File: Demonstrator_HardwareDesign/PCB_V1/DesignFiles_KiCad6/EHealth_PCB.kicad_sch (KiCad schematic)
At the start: 24 parts, among them J1-AnalogSensors1 Conn_01x05, J3-MagneticInterconnect1 Conn_01x08, J4-OffTheShelf-Digital1 Conn_02x06_Counter_Clockwise, J5-Power1 Conn_01x03

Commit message: aangepaste pcb layout
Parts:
- removed J1-AnalogSensors1: Conn_01x05, Connector_PinHeader_2.54mm:PinHeader_1x05_P2.54mm_Vertical, symbol Connector_Generic:Conn_01x05
- removed R10, R11, R12, R5, R6, R7, R8, R9: R, Resistor_SMD:R_0805_2012Metric_Pad1.20x1.40mm_HandSolder, symbol Device:R
- added J1: Conn_01x06, Connector_PinHeader_2.54mm:PinHeader_2x04_P2.54mm_Vertical, symbol Connector_Generic:Conn_01x08
- added R16, R17, R21, R22: R, Resistor_SMD:R_0805_2012Metric_Pad1.20x1.40mm_HandSolder, symbol Device:R
- J3-MagneticInterconnect1: footprint Connector_JST:JST_VH_B8P-VH-B_1x08_P3.96mm_Vertical -> Connector_JST:JST_VH_B4P-VH-B_1x04_P3.96mm_Vertical; symbol Connector_Generic:Conn_01x08 -> Connector_Generic:Conn_01x04
- J4-OffTheShelf-Digital1: footprint Connector_PinSocket_2.54mm:PinSocket_2x06_P2.54mm_Vertical -> Connector_PinSocket_2.54mm:PinSocket_2x04_P2.54mm_Vertical; symbol Connector_Generic:Conn_02x06_Counter_Clockwise -> Connector_Generic:Conn_02x04_Counter_Clockwise
- renumbered R16 to R18, R17 to R19, R18 to R20
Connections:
- net +3.3V: now also J1.1 (Pin_1), R16.2, R17.2
- net GND: now also J1.2 (Pin_2), J1.8 (Pin_8), R21.2, R22.2
- net SPI_CS: no longer J3-MagneticInterconnect1.8 (Pin_8), J4-OffTheShelf-Digital1.9 (Pin_9)
- net SPI_MISO: now also J1.7 (Pin_7), R17.1, R22.1; no longer J3-MagneticInterconnect1.5 (Pin_5), J4-OffTheShelf-Digital1.12 (Pin_12)
- net SPI_MOSI: now also R13.1, R18.1, J1.6 (Pin_6); no longer J3-MagneticInterconnect1.6 (Pin_6), J4-OffTheShelf-Digital1.11 (Pin_11)
- net SPI_SCK: now also J1.3 (Pin_3), R16.1, R21.1; no longer J3-MagneticInterconnect1.7 (Pin_7), J4-OffTheShelf-Digital1.10 (Pin_10)
- net at LOLIN_C3_PICO1.10 (3_-_A3_-_VBAT), R14.1, R19.1: now also J1.5 (Pin_5)
- net at LOLIN_C3_PICO1.11 (2_-_A2), R15.1, R20.1: now also J1.4 (Pin_4)
- now unconnected: LOLIN_C3_PICO1.15 (5_-_A5)
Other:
- moved on the sheet: C1, C2, J5-Power1, LOLIN_C3_PICO1, R1, R13, R14, R15, R18, R19, R2, R20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

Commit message: aangepaste layout
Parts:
- removed R1, R18, R19, R20, R21, R22: R, Resistor_SMD:R_0805_2012Metric_Pad1.20x1.40mm_HandSolder, symbol Device:R
- J1: footprint Connector_PinHeader_2.54mm:PinHeader_2x04_P2.54mm_Vertical -> Connector_PinHeader_2.54mm:PinHeader_2x05_P2.54mm_Vertical; symbol Connector_Generic:Conn_01x08 -> Connector_Generic:Conn_01x10
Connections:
- net +3.3V: no longer J1.1 (Pin_1), J3-MagneticInterconnect1.1 (Pin_1)
- net GND: now also J1.1 (Pin_1), J1.3 (Pin_3), J1.5 (Pin_5), J1.7 (Pin_7), J1.9 (Pin_9); no longer J1.2 (Pin_2), J1.8 (Pin_8)
- net SPI_CS: now also J4-OffTheShelf-Digital1.5 (Pin_5)
- net SPI_MISO: no longer J1.7 (Pin_7), LOLIN_C3_PICO1.13 (0_-_A0_-_MISO), R17.1
- net at LOLIN_C3_PICO1.10 (3_-_A3_-_VBAT), R14.1: now also J1.8 (Pin_8); no longer J1.5 (Pin_5)
- net at LOLIN_C3_PICO1.11 (2_-_A2), R15.1: now also J1.6 (Pin_6); no longer J1.4 (Pin_4)
- net SPI_MOSI: no longer names the net of LOLIN_C3_PICO1.14 (4_-_A4_-_MOSI), R13.1
- net SPI_MOSI: now also J1.10 (Pin_10); no longer J1.6 (Pin_6)
- net SPI_SCK: no longer names the net of LOLIN_C3_PICO1.12 (1_-_A1_-_SCK), R16.1
- net SPI_SCK: now also J1.4 (Pin_4); no longer J1.3 (Pin_3)
- new net: J1.2 (Pin_2), LOLIN_C3_PICO1.13 (0_-_A0_-_MISO), R17.1
- new net Vdd: J3-MagneticInterconnect1.1 (Pin_1)
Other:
- moved on the sheet: R13, R14, R15, R16, R17

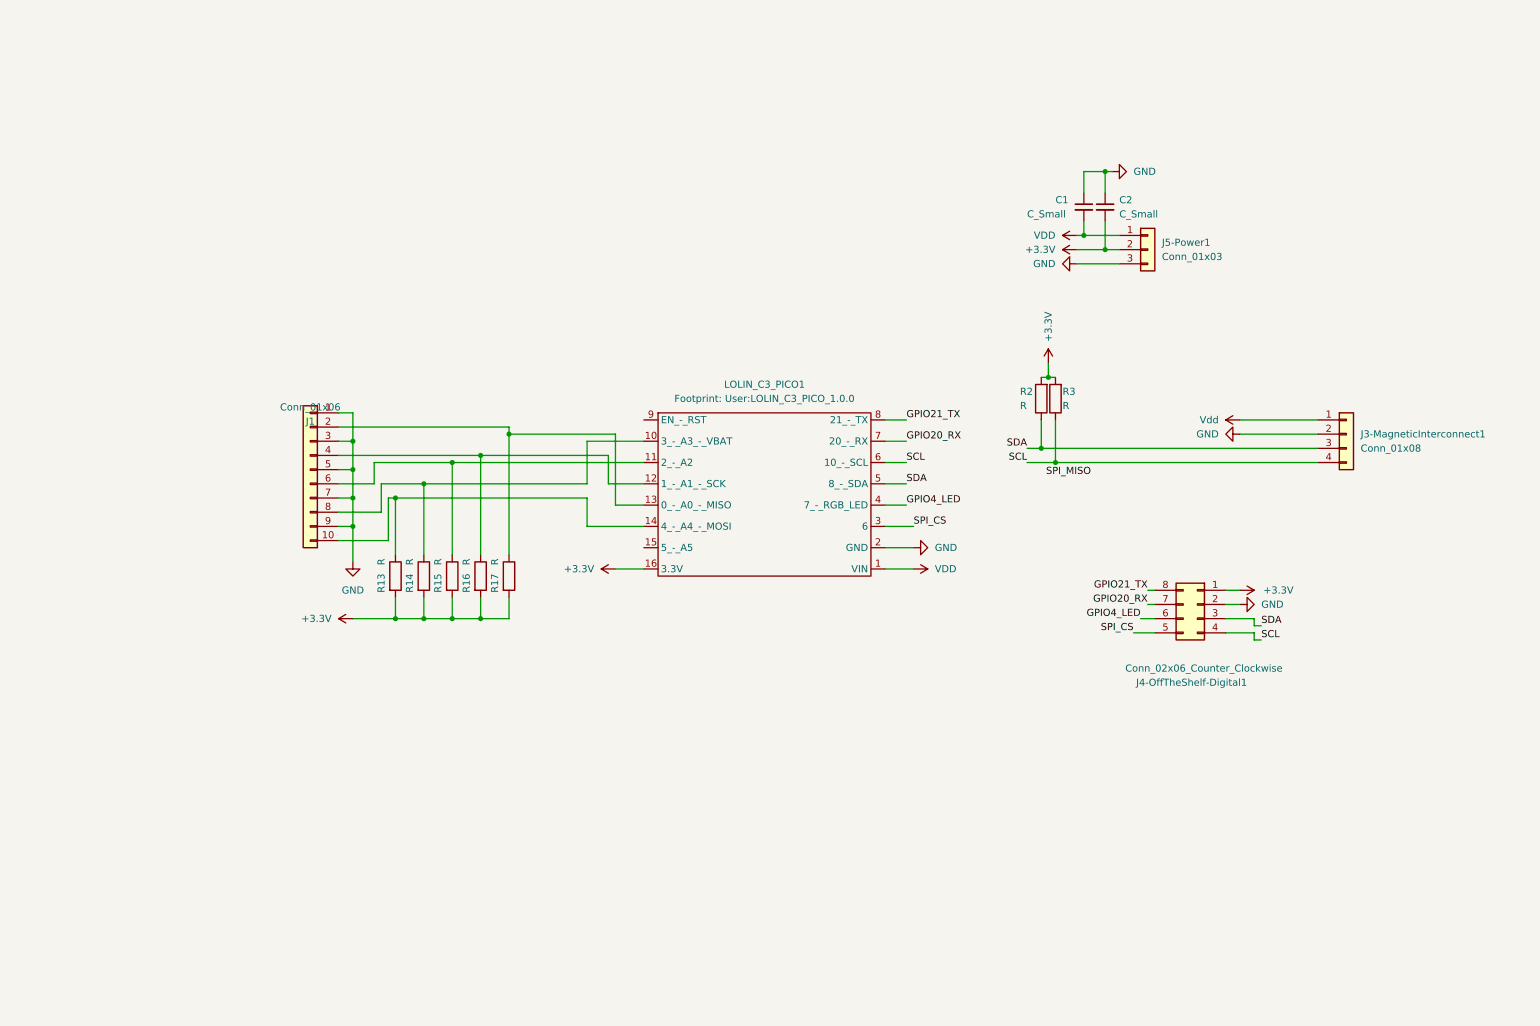
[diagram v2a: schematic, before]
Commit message: layout met buck en mult chip
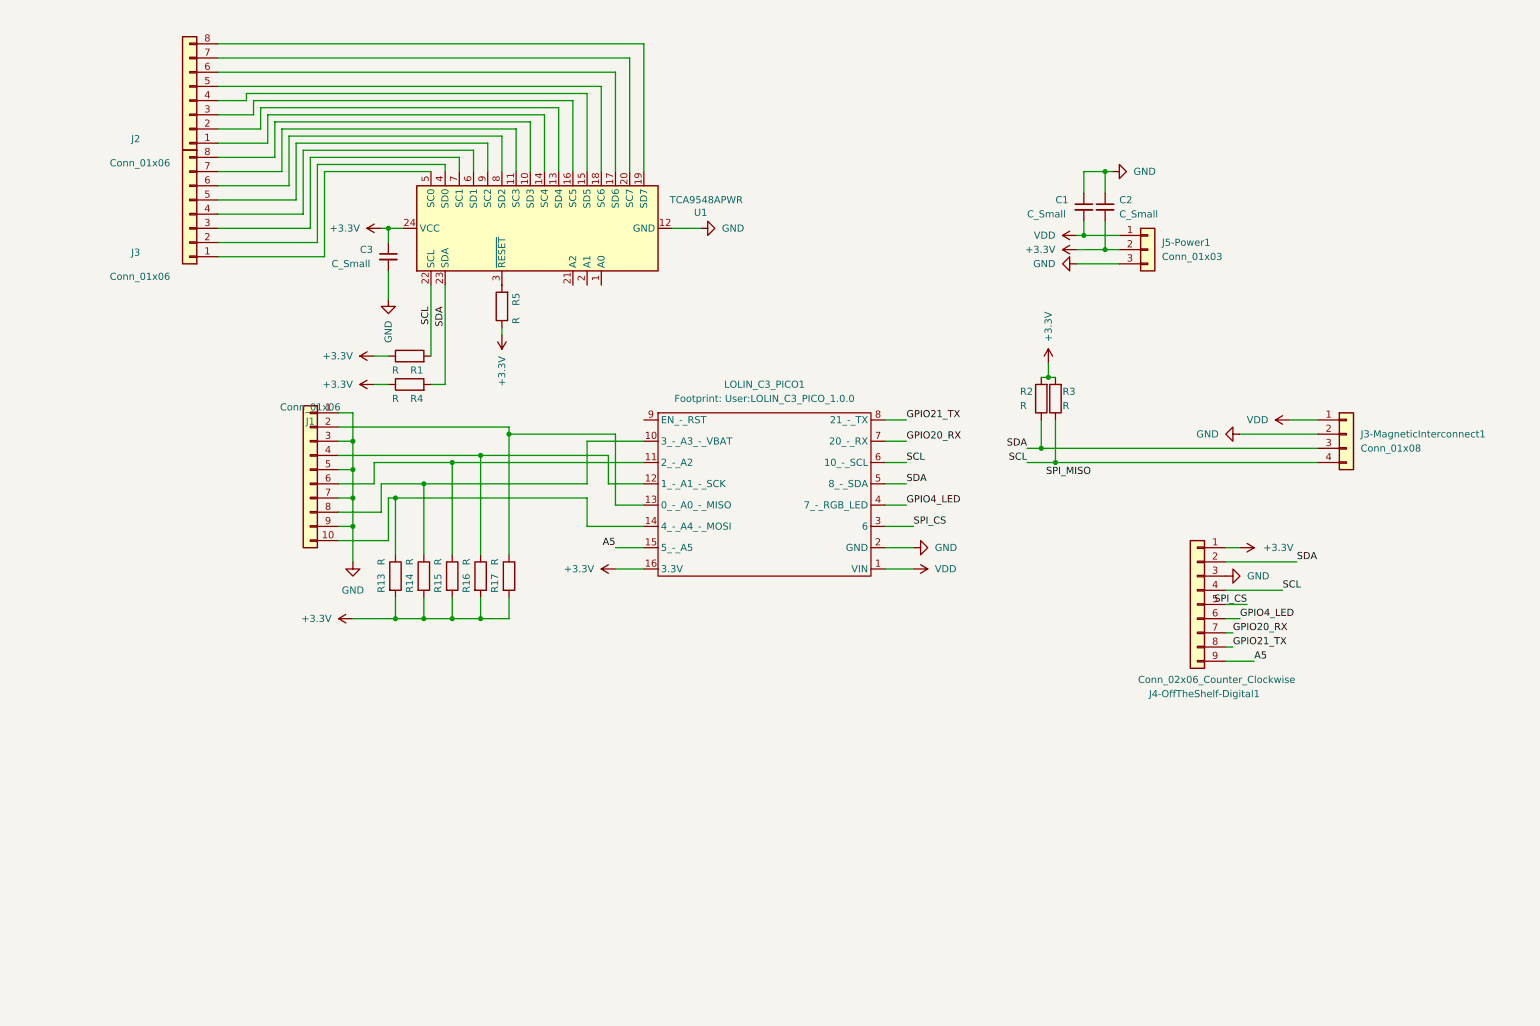
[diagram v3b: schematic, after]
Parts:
- added C3: C_Small, Capacitor_SMD:C_0805_2012Metric_Pad1.18x1.45mm_HandSolder, symbol Device:C_Small
- added J2, J3: Conn_01x06, Connector_PinHeader_2.54mm:PinHeader_2x04_P2.54mm_Vertical, symbol Connector_Generic:Conn_01x08
- added R1, R4, R5: R, Resistor_SMD:R_0805_2012Metric_Pad1.20x1.40mm_HandSolder, symbol Device:R
- added U1: TCA9548APWR, Package_SO:TSSOP-24_4.4x7.8mm_P0.65mm, symbol Interface_Expansion:TCA9548APWR
- J4-OffTheShelf-Digital1: footprint Connector_PinSocket_2.54mm:PinSocket_2x04_P2.54mm_Vertical -> Connector_PinHeader_2.54mm:PinHeader_2x05_P2.54mm_Vertical; symbol Connector_Generic:Conn_02x04_Counter_Clockwise -> Connector_Generic:Conn_01x09
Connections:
- net Vdd is gone; now on net VDD: J3-MagneticInterconnect1.1 (Pin_1)
- net +3.3V: now also C3.1, R1.1, R4.1, R5.1, U1.24 (VCC)
- net GND: now also J4-OffTheShelf-Digital1.3 (Pin_3), C3.2, U1.12 (GND); no longer J4-OffTheShelf-Digital1.2 (Pin_2)
- net SCL: now also R1.2, U1.22 (SCL)
- net SDA: now also J4-OffTheShelf-Digital1.2 (Pin_2), R4.2, U1.23 (SDA); no longer J4-OffTheShelf-Digital1.3 (Pin_3)
- net A5: now reaches LOLIN_C3_PICO1.15 (5_-_A5)
- net A5: now also J4-OffTheShelf-Digital1.9 (Pin_9)
- new net: J2.1 (Pin_1), U1.14 (SC4)
- new net: J2.2 (Pin_2), U1.13 (SD4)
- new net: J2.3 (Pin_3), U1.16 (SC5)
- new net: J2.4 (Pin_4), U1.15 (SD5)
- new net: J2.5 (Pin_5), U1.18 (SC6)
- new net: J2.6 (Pin_6), U1.17 (SD6)
- new net: J2.7 (Pin_7), U1.20 (SC7)
- new net: J2.8 (Pin_8), U1.19 (SD7)
- new net: R5.2, U1.3 (~{RESET})
- new net: J3.8 (Pin_8), U1.10 (SD3)
- new net: J3.7 (Pin_7), U1.11 (SC3)
- new net: J3.2 (Pin_2), U1.4 (SD0)
- new net: J3.1 (Pin_1), U1.5 (SC0)
- new net: J3.4 (Pin_4), U1.6 (SD1)
- new net: J3.3 (Pin_3), U1.7 (SC1)
- new net: J3.6 (Pin_6), U1.8 (SD2)
- new net: J3.5 (Pin_5), U1.9 (SC2)

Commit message: schema met mult chip en buck convertor
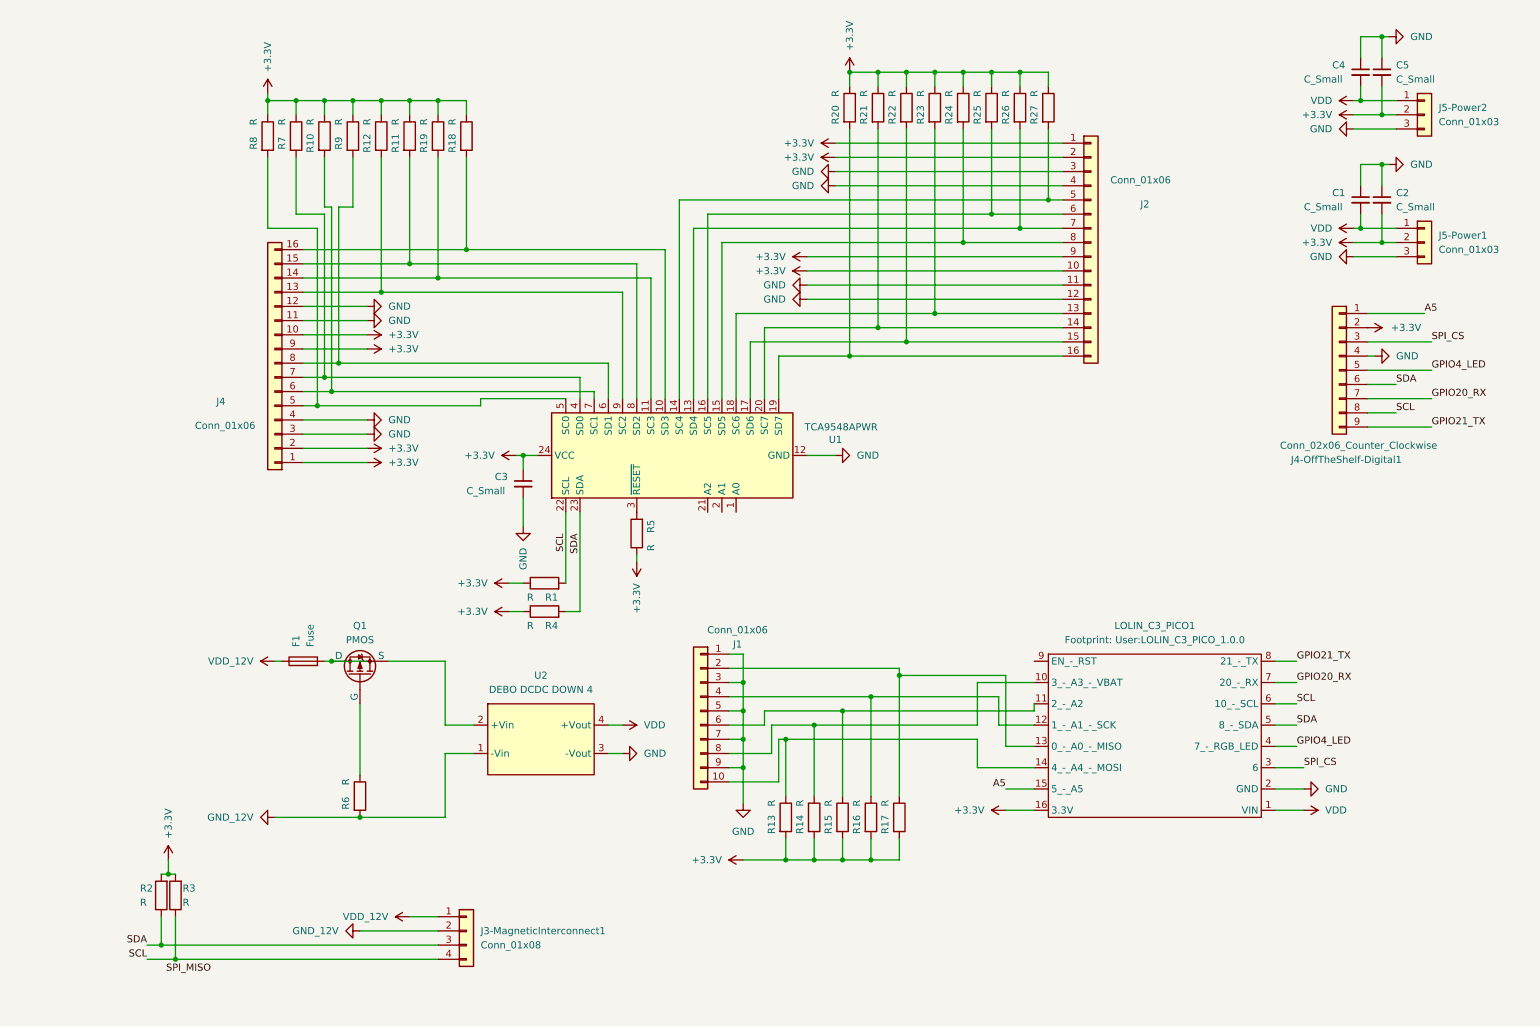
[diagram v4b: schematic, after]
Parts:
- removed J2, J3: Conn_01x06, Connector_PinHeader_2.54mm:PinHeader_2x04_P2.54mm_Vertical, symbol Connector_Generic:Conn_01x08
- added C4, C5: C_Small, Capacitor_SMD:C_0805_2012Metric_Pad1.18x1.45mm_HandSolder, symbol Device:C_Small
- added F1: Fuse, Fuse:Fuse_0402_1005Metric, symbol Device:Fuse
- added J2: Conn_01x06, Connector_PinHeader_2.54mm:PinHeader_1x16_P2.54mm_Vertical, symbol Connector_Generic:Conn_01x16
- added J4: Conn_01x06, Connector_PinHeader_2.54mm:PinHeader_2x08_P2.54mm_Vertical, symbol Connector_Generic:Conn_01x16
- added J5-Power2: Conn_01x03, Connector_PinSocket_2.54mm:PinSocket_1x03_P2.54mm_Vertical, symbol Connector_Generic:Conn_01x03
- added Q1: PMOS, Package_TO_SOT_SMD:SOT-23_Handsoldering, symbol Simulation_SPICE:PMOS
- added R10, R11, R12, R18, R19, R20, R21, R22, R23, R24, R25, R26, R27, R6, R7, R8, R9: R, Resistor_SMD:R_0805_2012Metric_Pad1.20x1.40mm_HandSolder, symbol Device:R
- added U2: DEBO DCDC DOWN 4, DEBO DCDC DOWN 4:DEBO DCDC DOWN 4, symbol buck_convertor:DEBO_DCDC_DOWN_4
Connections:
- net +3.3V: now also J4-OffTheShelf-Digital1.2 (Pin_2), C5.2, J2.1 (Pin_1), J2.10 (Pin_10), J2.2 (Pin_2), J2.9 (Pin_9), J4.1 (Pin_1), J4.10 (Pin_10), J4.2 (Pin_2), J4.9 (Pin_9), J5-Power2.2 (Pin_2), R10.1, R11.1, R12.1, R18.1, R19.1, R20.1, R21.1, R22.1, R23.1, R24.1, R25.1, R26.1, R27.1, R7.1, R8.1, R9.1; no longer J4-OffTheShelf-Digital1.1 (Pin_1)
- net A5: now also J4-OffTheShelf-Digital1.1 (Pin_1); no longer J4-OffTheShelf-Digital1.9 (Pin_9)
- net GND: now also J4-OffTheShelf-Digital1.4 (Pin_4), C4.1, C5.1, J2.11 (Pin_11), J2.12 (Pin_12), J2.3 (Pin_3), J2.4 (Pin_4), J4.11 (Pin_11), J4.12 (Pin_12), J4.3 (Pin_3), J4.4 (Pin_4), J5-Power2.3 (Pin_3), U2.3 (-Vout); no longer J3-MagneticInterconnect1.2 (Pin_2), J4-OffTheShelf-Digital1.3 (Pin_3)
- net GPIO21_TX: now also J4-OffTheShelf-Digital1.9 (Pin_9); no longer J4-OffTheShelf-Digital1.8 (Pin_8)
- net GPIO4_LED: now also J4-OffTheShelf-Digital1.5 (Pin_5); no longer J4-OffTheShelf-Digital1.6 (Pin_6)
- net SCL: now also J4-OffTheShelf-Digital1.8 (Pin_8); no longer J4-OffTheShelf-Digital1.4 (Pin_4)
- net SDA: now also J4-OffTheShelf-Digital1.6 (Pin_6); no longer J4-OffTheShelf-Digital1.2 (Pin_2)
- net SPI_CS: now also J4-OffTheShelf-Digital1.3 (Pin_3); no longer J4-OffTheShelf-Digital1.5 (Pin_5)
- net VDD: now also C4.2, J5-Power2.1 (Pin_1), U2.4 (+Vout); no longer J3-MagneticInterconnect1.1 (Pin_1)
- net at U1.14 (SC4): now also J2.5 (Pin_5), R27.2
- net at U1.13 (SD4): now also J2.7 (Pin_7), R26.2
- net at U1.16 (SC5): now also J2.6 (Pin_6), R25.2
- net at U1.15 (SD5): now also J2.8 (Pin_8), R24.2
- net at U1.18 (SC6): now also J2.13 (Pin_13), R23.2
- net at U1.17 (SD6): now also J2.15 (Pin_15), R22.2
- net at U1.20 (SC7): now also J2.14 (Pin_14), R21.2
- net at U1.19 (SD7): now also J2.16 (Pin_16), R20.2
- net at U1.10 (SD3): now also J4.16 (Pin_16), R18.2
- net at U1.11 (SC3): now also J4.14 (Pin_14), R19.2
- net at U1.4 (SD0): now also J4.7 (Pin_7), R7.2
- net at U1.5 (SC0): now also J4.5 (Pin_5), R8.2
- net at U1.6 (SD1): now also J4.8 (Pin_8), R9.2
- net at U1.7 (SC1): now also J4.6 (Pin_6), R10.2
- net at U1.8 (SD2): now also J4.15 (Pin_15), R11.2
- net at U1.9 (SC2): now also J4.13 (Pin_13), R12.2
- new net: Q1.2 (G), R6.1
- new net: Q1.3 (S), U2.2 (+Vin)
- new net: F1.2, Q1.1 (D)
- new net GND_12V: J3-MagneticInterconnect1.2 (Pin_2), R6.2, U2.1 (-Vin)
- new net VDD_12V: F1.1, J3-MagneticInterconnect1.1 (Pin_1)
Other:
- moved on the sheet: C1, C2, C3, J1, J3-MagneticInterconnect1, J4-OffTheShelf-Digital1, J5-Power1, LOLIN_C3_PICO1, R1, R13, R14, R15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

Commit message: up to date
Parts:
- F1: footprint Fuse:Fuse_0402_1005Metric -> Fuse:Fuse_0805_2012Metric_Pad1.15x1.40mm_HandSolder
- Q1: footprint Package_TO_SOT_SMD:SOT-23_Handsoldering -> Package_SO:Infineon_PG-DSO-8-27_3.9x4.9mm_EP2.65x3mm
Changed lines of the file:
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@@
 	)
 	(junction
-		(at 68.58 132.08)
-		(diameter 0)
-		(color 0 0 0 0)
-	)
-	(junction
 		(at 161.29 26.67)
 		(diameter 0)
@@
 	(wire
 		(pts
-			(xy 74.93 132.08) (xy 68.58 132.08)
-		)
-		(stroke
-			(width 0)
-			(type default)
-		)
-	)
-	(wire
-		(pts
 			(xy 251.46 31.75) (xy 252.73 31.75)
 		)
@@
 			)
 		)
-		(property "Footprint" "Package_TO_SOT_SMD:SOT-23_Handsoldering"
+		(property "Footprint" "Package_SO:Infineon_PG-DSO-8-27_3.9x4.9mm_EP2.65x3mm"
 			(at 71.12 129.54 0)
 			(effects
@@
 			)
 		)
-		(property "Footprint" "Fuse:Fuse_0402_1005Metric"
+		(property "Footprint" "Fuse:Fuse_0805_2012Metric_Pad1.15x1.40mm_HandSolder"
 			(at 63.5 133.858 90)
 			(effects

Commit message: huidige layout
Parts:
- removed J2: Conn_01x06, Connector_PinHeader_2.54mm:PinHeader_1x16_P2.54mm_Vertical, symbol Connector_Generic:Conn_01x16
- added D1, D4, D5: TVS Diode 824012823, Resistor_SMD:R_0603_1608Metric_Pad0.98x0.95mm_HandSolder, symbol Diode:SMAJ250CA
- added D2, D3, D6: TVS Diode 824012823, Resistor_SMD:R_0603_1608Metric_Pad0.98x0.95mm_HandSolder, symbol Diode:SMAJ400CA
- added FB1, FB2, FB3, FB4, FB5, FB6: FerriteBead, Resistor_SMD:R_0805_2012Metric_Pad1.20x1.40mm_HandSolder, symbol Device:FerriteBead
- added J2, J3: Conn_01x06, Connector_PinHeader_2.54mm:PinHeader_1x08_P2.54mm_Vertical, symbol Connector_Generic:Conn_01x08
- Q1: footprint Package_SO:Infineon_PG-DSO-8-27_3.9x4.9mm_EP2.65x3mm -> Library-TRANS:PG-TDSON-8
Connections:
- net +3.3V: now also J2.1 (Pin_1), J2.5 (Pin_5), J3.1 (Pin_1), J3.5 (Pin_5)
- net GND: now also D1.1 (A1), D2.1 (A1), D3.1 (A1), D4.1 (A1), D5.1 (A1), D6.1 (A1), J2.2 (Pin_2), J2.6 (Pin_6), J3.2 (Pin_2), J3.6 (Pin_6)
- net SCL: now also FB2.2; no longer J3-MagneticInterconnect1.4 (Pin_4)
- net SDA: now also FB1.1; no longer J3-MagneticInterconnect1.3 (Pin_3)
- net at J1.8 (Pin_8), R14.1: now also LOLIN_C3_PICO1.13 (0_-_A0_-_MISO); no longer LOLIN_C3_PICO1.10 (3_-_A3_-_VBAT)
- net at J1.6 (Pin_6), R15.1: now also LOLIN_C3_PICO1.12 (1_-_A1_-_SCK); no longer LOLIN_C3_PICO1.11 (2_-_A2)
- net at J1.4 (Pin_4), R16.1: now also LOLIN_C3_PICO1.11 (2_-_A2); no longer LOLIN_C3_PICO1.12 (1_-_A1_-_SCK)
- net at J1.2 (Pin_2), R17.1: now also LOLIN_C3_PICO1.10 (3_-_A3_-_VBAT); no longer LOLIN_C3_PICO1.13 (0_-_A0_-_MISO)
- net at U1.20 (SC7): now also R22.2, J3.3 (Pin_3); no longer R21.2
- net at R23.2: now also U1.19 (SD7), J3.4 (Pin_4); no longer U1.18 (SC6)
- net at U1.17 (SD6): now also R21.2, J3.8 (Pin_8); no longer R22.2
- net at R20.2: now also U1.18 (SC6), J3.7 (Pin_7); no longer U1.19 (SD7)
- net at U1.14 (SC4): now also R24.2, J2.7 (Pin_7); no longer R27.2
- net at U1.16 (SC5): now also R26.2, J2.3 (Pin_3); no longer R25.2
- net at U1.13 (SD4): now also R25.2, J2.8 (Pin_8); no longer R26.2
- net at U1.15 (SD5): now also R27.2, J2.4 (Pin_4); no longer R24.2
- net at J4.13 (Pin_13), R12.2: now also D6.2 (A2), FB6.2; no longer U1.9 (SC2)
- net at J4.15 (Pin_15), R11.2: now also D5.2 (A2), FB5.2; no longer U1.8 (SD2)
- net at J4.7 (Pin_7), R7.2: now also D4.2 (A2), FB4.2; no longer U1.4 (SD0)
- net at J4.5 (Pin_5), R8.2: now also D3.2 (A2), FB3.2; no longer U1.5 (SC0)
- new net: D2.2 (A2), FB1.2, J3-MagneticInterconnect1.3 (Pin_3)
- new net: D1.2 (A2), FB2.1, J3-MagneticInterconnect1.4 (Pin_4)
- new net: FB3.1, U1.5 (SC0)
- new net: FB4.1, U1.4 (SD0)
- new net: FB6.1, U1.9 (SC2)
- new net: FB5.1, U1.8 (SD2)
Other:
- moved on the sheet: J3-MagneticInterconnect1, J4, R10, R11, R12, R18, R19, R2, R3, R7, R8, R9
